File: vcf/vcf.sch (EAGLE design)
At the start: 94 parts, among them IC1 OPA4130U, IC2 OPA4130U, IC3 OPA4130U, IC4 OPA4130U, IC5 OPA4130U, Q1 BC847ASMD, Q2 BC847ASMD, Q3 BC847ASMD, Q4 BC847ASMD, Q5 BC847ASMD, Q6 BC847ASMD

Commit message: added some critical stuff.  sent the board to pcbway for checking.
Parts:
- added R47, R48: 1k, dan:R-US_R0603
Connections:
- new net N$65: FREQ.A, R48.2
- new net N$66: FREQ.E, R47.1
- net +12V: now also R47.2; no longer FREQ.E
- net -12V: now also R48.1; no longer FREQ.A
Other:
- moved on the sheet: FREQ, R25, R44
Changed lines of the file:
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@@
 <part name="R45" library="dan" deviceset="R-US_" device="R0603" value="1k"/>
 <part name="R46" library="dan" deviceset="R-US_" device="R0603" value="1k"/>
+<part name="R47" library="dan" deviceset="R-US_" device="R0603" value="1k"/>
+<part name="R48" library="dan" deviceset="R-US_" device="R0603" value="1k"/>
 </parts>
 <sheets>
@@
 <instance part="R23" gate="G$1" x="-20.32" y="-33.02"/>
 <instance part="R24" gate="G$1" x="-48.26" y="-53.34"/>
-<instance part="R25" gate="G$1" x="-68.58" y="-35.56"/>
+<instance part="R25" gate="G$1" x="-68.58" y="-43.18"/>
 <instance part="R26" gate="G$1" x="-68.58" y="-53.34"/>
 <instance part="MODAMT" gate="G$1" x="-99.06" y="-25.4"/>
@@
 <instance part="GND20" gate="1" x="208.28" y="73.66"/>
 <instance part="GND21" gate="1" x="149.86" y="200.66"/>
-<instance part="FREQ" gate="G$1" x="-78.74" y="-12.7"/>
-<instance part="P-7" gate="1" x="-78.74" y="-25.4"/>
-<instance part="P+9" gate="1" x="-78.74" y="0"/>
-<instance part="R44" gate="G$1" x="-66.04" y="-12.7"/>
+<instance part="FREQ" gate="G$1" x="-78.74" y="-15.24"/>
+<instance part="P-7" gate="1" x="-78.74" y="-40.64"/>
+<instance part="P+9" gate="1" x="-78.74" y="10.16"/>
+<instance part="R44" gate="G$1" x="-66.04" y="-15.24"/>
 <instance part="GAIN1" gate="G$1" x="-99.06" y="5.08"/>
 <instance part="C5" gate="G$1" x="-2.54" y="38.1" rot="R270"/>
@@
 <instance part="R45" gate="G$1" x="205.74" y="66.04" rot="R180"/>
 <instance part="R46" gate="G$1" x="147.32" y="193.04" rot="R180"/>
+<instance part="R47" gate="G$1" x="-78.74" y="0" rot="R90"/>
+<instance part="R48" gate="G$1" x="-78.74" y="-30.48" rot="R90"/>
 </instances>
 <busses>
@@
 </segment>
 <segment>
-<pinref part="FREQ" gate="G$1" pin="E"/>
-<pinref part="P+9" gate="1" pin="+12V"/>
-<wire x1="-78.74" y1="-5.08" x2="-78.74" y2="-2.54" width="0.1524" layer="91"/>
-</segment>
-<segment>
 <pinref part="P+10" gate="1" pin="+12V"/>
 <wire x1="-12.7" y1="154.94" x2="-12.7" y2="152.4" width="0.1524" layer="91"/>
@@
 <pinref part="P+7" gate="1" pin="+12V"/>
 </segment>
+<segment>
+<pinref part="R47" gate="G$1" pin="2"/>
+<pinref part="P+9" gate="1" pin="+12V"/>
+<wire x1="-78.74" y1="7.62" x2="-78.74" y2="5.08" width="0.1524" layer="91"/>
+</segment>
 </net>
 <net name="-12V" class="0">
@@
 <wire x1="-50.8" y1="177.8" x2="-40.64" y2="177.8" width="0.1524" layer="91"/>
 <junction x="-50.8" y="177.8"/>
-</segment>
-<segment>
-<pinref part="P-7" gate="1" pin="-12V"/>
-<pinref part="FREQ" gate="G$1" pin="A"/>
-<wire x1="-78.74" y1="-22.86" x2="-78.74" y2="-20.32" width="0.1524" layer="91"/>
 </segment>
 <segment>
@@
 <pinref part="P-5" gate="1" pin="-12V"/>
 </segment>
+<segment>
+<pinref part="P-7" gate="1" pin="-12V"/>
+<pinref part="R48" gate="G$1" pin="1"/>
+<wire x1="-78.74" y1="-38.1" x2="-78.74" y2="-35.56" width="0.1524" layer="91"/>
+</segment>
 </net>
 <net name="N$17" class="0">
@@
 <wire x1="-63.5" y1="-53.34" x2="-58.42" y2="-53.34" width="0.1524" layer="91"/>
 <junction x="-58.42" y="-53.34"/>
-<wire x1="-58.42" y1="-35.56" x2="-58.42" y2="-53.34" width="0.1524" layer="91"/>
+<wire x1="-58.42" y1="-35.56" x2="-58.42" y2="-43.18" width="0.1524" layer="91"/>
+<wire x1="-58.42" y1="-43.18" x2="-58.42" y2="-53.34" width="0.1524" layer="91"/>
+<wire x1="-53.34" y1="-35.56" x2="-58.42" y2="-35.56" width="0.1524" layer="91"/>
+<pinref part="IC5" gate="B" pin="-IN"/>
 <pinref part="R25" gate="G$1" pin="2"/>
-<wire x1="-63.5" y1="-35.56" x2="-58.42" y2="-35.56" width="0.1524" layer="91"/>
-<wire x1="-53.34" y1="-35.56" x2="-58.42" y2="-35.56" width="0.1524" layer="91"/>
-<junction x="-58.42" y="-35.56"/>
-<pinref part="IC5" gate="B" pin="-IN"/>
+<wire x1="-63.5" y1="-43.18" x2="-58.42" y2="-43.18" width="0.1524" layer="91"/>
+<junction x="-58.42" y="-43.18"/>
 </segment>
 </net>
@@
 <net name="N$40" class="0">
 <segment>
-<pinref part="R25" gate="G$1" pin="1"/>
-<wire x1="-73.66" y1="-35.56" x2="-83.82" y2="-35.56" width="0.1524" layer="91"/>
-<wire x1="-83.82" y1="-35.56" x2="-83.82" y2="-25.4" width="0.1524" layer="91"/>
+<wire x1="-83.82" y1="-43.18" x2="-83.82" y2="-25.4" width="0.1524" layer="91"/>
 <pinref part="MODAMT" gate="G$1" pin="S"/>
 <wire x1="-83.82" y1="-25.4" x2="-93.98" y2="-25.4" width="0.1524" layer="91"/>
+<pinref part="R25" gate="G$1" pin="1"/>
+<wire x1="-73.66" y1="-43.18" x2="-83.82" y2="-43.18" width="0.1524" layer="91"/>
 </segment>
 </net>
@@
 <pinref part="FREQ" gate="G$1" pin="S"/>
 <pinref part="R44" gate="G$1" pin="1"/>
-<wire x1="-73.66" y1="-12.7" x2="-71.12" y2="-12.7" width="0.1524" layer="91"/>
+<wire x1="-73.66" y1="-15.24" x2="-71.12" y2="-15.24" width="0.1524" layer="91"/>
 </segment>
 </net>
 <net name="N$62" class="0">
 <segment>
-<wire x1="-73.66" y1="5.08" x2="-73.66" y2="20.32" width="0.1524" layer="91"/>
+<wire x1="-88.9" y1="5.08" x2="-88.9" y2="20.32" width="0.1524" layer="91"/>
 <pinref part="R20" gate="G$1" pin="1"/>
-<wire x1="-73.66" y1="20.32" x2="-71.12" y2="20.32" width="0.1524" layer="91"/>
+<wire x1="-88.9" y1="20.32" x2="-71.12" y2="20.32" width="0.1524" layer="91"/>
 <pinref part="GAIN1" gate="G$1" pin="S"/>
-<wire x1="-93.98" y1="5.08" x2="-73.66" y2="5.08" width="0.1524" layer="91"/>
+<wire x1="-93.98" y1="5.08" x2="-88.9" y2="5.08" width="0.1524" layer="91"/>
 </segment>
 </net>
@@
 <pinref part="IC5" gate="B" pin="+IN"/>
 <pinref part="R44" gate="G$1" pin="2"/>
-<wire x1="-58.42" y1="-12.7" x2="-60.96" y2="-12.7" width="0.1524" layer="91"/>
-<wire x1="-58.42" y1="-30.48" x2="-58.42" y2="-12.7" width="0.1524" layer="91"/>
+<wire x1="-58.42" y1="-15.24" x2="-60.96" y2="-15.24" width="0.1524" layer="91"/>
+<wire x1="-58.42" y1="-30.48" x2="-58.42" y2="-15.24" width="0.1524" layer="91"/>
 </segment>
 </net>
@@
 </segment>
 </net>
+<net name="N$65" class="0">
+<segment>
+<pinref part="FREQ" gate="G$1" pin="A"/>
+<pinref part="R48" gate="G$1" pin="2"/>
+<wire x1="-78.74" y1="-25.4" x2="-78.74" y2="-22.86" width="0.1524" layer="91"/>
+</segment>
+</net>
+<net name="N$66" class="0">
+<segment>
+<pinref part="FREQ" gate="G$1" pin="E"/>
+<pinref part="R47" gate="G$1" pin="1"/>
+<wire x1="-78.74" y1="-5.08" x2="-78.74" y2="-7.62" width="0.1524" layer="91"/>
+</segment>
+</net>

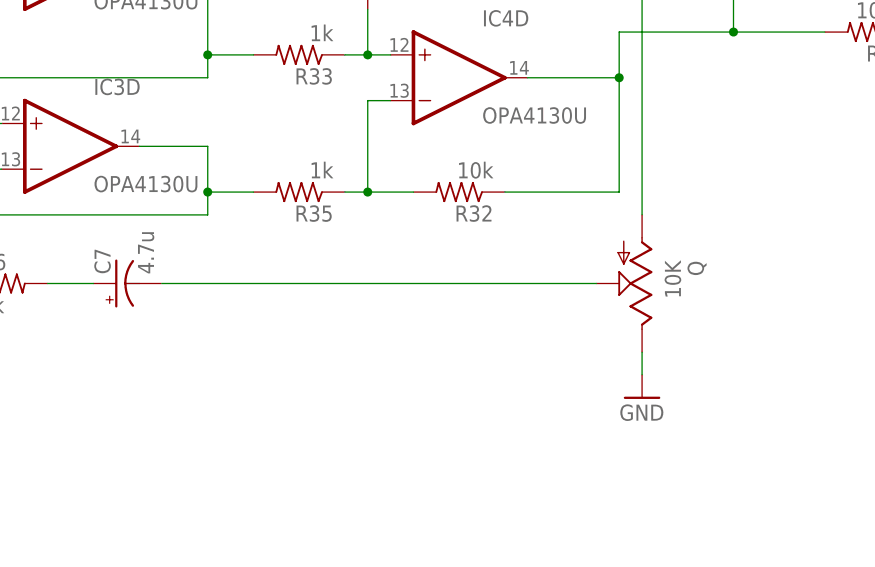
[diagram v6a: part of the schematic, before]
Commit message: fixed polarity on resonance pot.  Sent out to fab.
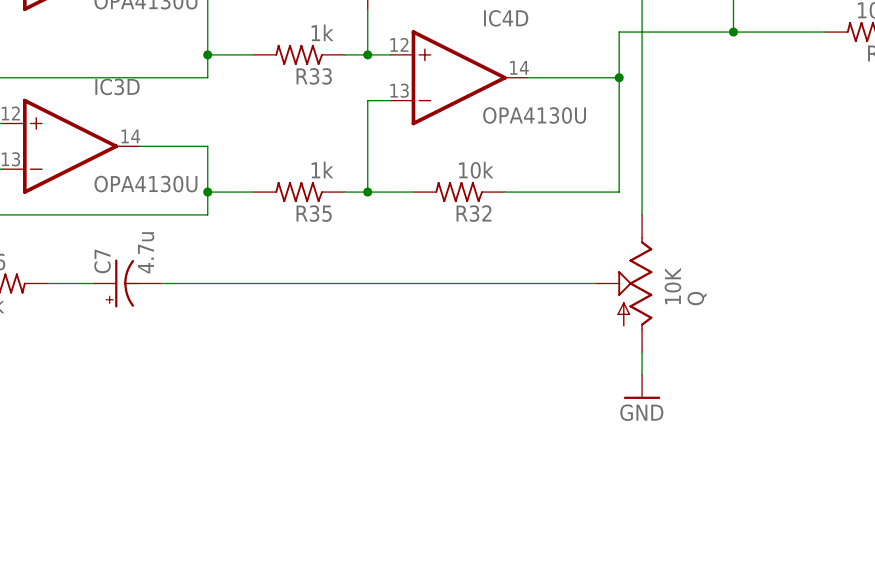
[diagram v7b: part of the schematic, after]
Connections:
- net GND: now also Q.A; no longer Q.E
- net N$27: now also Q.E; no longer Q.A
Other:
- moved on the sheet: Q
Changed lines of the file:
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@@
 <instance part="GND5" gate="1" x="101.6" y="215.9"/>
 <instance part="R16" gate="G$1" x="68.58" y="38.1"/>
-<instance part="Q" gate="G$1" x="139.7" y="38.1" rot="R180"/>
+<instance part="Q" gate="G$1" x="139.7" y="38.1" rot="MR0"/>
 <instance part="R18" gate="G$1" x="-45.72" y="20.32"/>
 <instance part="R19" gate="G$1" x="-66.04" y="35.56"/>
@@
 </segment>
 <segment>
-<pinref part="Q" gate="G$1" pin="E"/>
-<pinref part="GND24" gate="1" pin="GND"/>
-<wire x1="139.7" y1="30.48" x2="139.7" y2="27.94" width="0.1524" layer="91"/>
-</segment>
-<segment>
 <pinref part="GND26" gate="1" pin="GND"/>
 <pinref part="GAIN" gate="G$1" pin="A"/>
@@
 <pinref part="GND10" gate="1" pin="GND"/>
 <wire x1="-142.24" y1="-53.34" x2="-142.24" y2="-55.88" width="0.1524" layer="91"/>
+</segment>
+<segment>
+<pinref part="Q" gate="G$1" pin="A"/>
+<pinref part="GND24" gate="1" pin="GND"/>
+<wire x1="139.7" y1="30.48" x2="139.7" y2="27.94" width="0.1524" layer="91"/>
 </segment>
 </net>
@@
 <pinref part="XPAND" gate="-10" pin="KL"/>
 <wire x1="172.72" y1="160.02" x2="139.7" y2="160.02" width="0.1524" layer="91"/>
-<pinref part="Q" gate="G$1" pin="A"/>
-<wire x1="139.7" y1="45.72" x2="139.7" y2="160.02" width="0.1524" layer="91"/>
-<junction x="139.7" y="160.02"/>
 <wire x1="139.7" y1="190.5" x2="139.7" y2="193.04" width="0.1524" layer="91"/>
 <wire x1="139.7" y1="193.04" x2="139.7" y2="203.2" width="0.1524" layer="91"/>
@@
 <wire x1="142.24" y1="193.04" x2="139.7" y2="193.04" width="0.1524" layer="91"/>
 <junction x="139.7" y="193.04"/>
+<pinref part="Q" gate="G$1" pin="E"/>
+<wire x1="139.7" y1="45.72" x2="139.7" y2="160.02" width="0.1524" layer="91"/>
+<junction x="139.7" y="160.02"/>
 </segment>
 </net>
@@
 </segment>
 </net>
-<net name="N$32" class="0">
-<segment>
-<pinref part="Q" gate="G$1" pin="S"/>
-<wire x1="86.36" y1="38.1" x2="134.62" y2="38.1" width="0.1524" layer="91"/>
-<pinref part="C7" gate="G$1" pin="-"/>
-</segment>
-</net>
 <net name="N$57" class="0">
 <segment>
@@
 </segment>
 </net>
+<net name="N$32" class="0">
+<segment>
+<pinref part="Q" gate="G$1" pin="S"/>
+<pinref part="C7" gate="G$1" pin="-"/>
+<wire x1="134.62" y1="38.1" x2="86.36" y2="38.1" width="0.1524" layer="91"/>
+</segment>
+</net>

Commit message: made some of the post first draft schematic changes
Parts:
- added R49, R50: 1k, dan:R-US_R0603
- R16: value 10k -> 1k
- R23: value 1k -> 100k
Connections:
- removed net N$65 (its old number): FREQ.A, R48.2
- new net N$60: FREQ.A, R47.1
- new net N$68: C6.1, R11.2, R49.1, R5.2, R50.2, R6.2
- net +12V: now also R50.1
- net N$13: now also R49.2; no longer C6.1, R11.2, R5.2, R6.2
- net N$66: now also R48.2; no longer R47.1
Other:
- note added: "Changed this to 50k, but it can be made small by moving them buffers"
- note added: "Freq pot polarity is wrong"
- note added: "Move the buffers after the pots"
- note added: "THis is really far away from the current pair"
- note added: "This was a big screwup"
- moved on the sheet: FREQ, R5
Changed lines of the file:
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@@
 <part name="R15" library="dan" deviceset="R-US_" device="R0603" value="10k"/>
 <part name="GND5" library="dan" deviceset="GND" device=""/>
-<part name="R16" library="dan" deviceset="R-US_" device="R0603" value="10k"/>
+<part name="R16" library="dan" deviceset="R-US_" device="R0603" value="1k"/>
 <part name="Q" library="dan" deviceset="US-EVU" device="F2J" value="10K"/>
 <part name="R18" library="dan" deviceset="R-US_" device="R0603" value="1k"/>
@@
 <part name="R22" library="dan" deviceset="R-US_" device="R0603" value="1k"/>
 <part name="GND9" library="dan" deviceset="GND" device=""/>
-<part name="R23" library="dan" deviceset="R-US_" device="R0603" value="1k"/>
+<part name="R23" library="dan" deviceset="R-US_" device="R0603" value="100k"/>
 <part name="R24" library="dan" deviceset="R-US_" device="R0603" value="1.2k"/>
 <part name="R25" library="dan" deviceset="R-US_" device="R0603" value="10k"/>
@@
 <part name="R47" library="dan" deviceset="R-US_" device="R0603" value="1k"/>
 <part name="R48" library="dan" deviceset="R-US_" device="R0603" value="1k"/>
+<part name="R49" library="dan" deviceset="R-US_" device="R0603" value="1k"/>
+<part name="P+11" library="dan" deviceset="+12V" device=""/>
+<part name="R50" library="dan" deviceset="R-US_" device="R0603" value="1k"/>
 </parts>
 <sheets>
@@
 <text x="2.54" y="208.28" size="3.81" layer="91">Double check this polarity</text>
 <text x="58.42" y="-35.56" size="3.81" layer="91">Double check this polarity</text>
+<text x="-137.16" y="-60.96" size="1.778" layer="91">Move the buffers after the pots</text>
+<text x="-137.16" y="-33.02" size="1.778" layer="91">Move the buffers after the pots</text>
+<text x="-71.12" y="-5.08" size="1.778" layer="91">Freq pot polarity is wrong</text>
+<text x="-68.58" y="-60.96" size="1.778" layer="91">THis is really far away from the current pair</text>
+<text x="-86.36" y="-63.5" size="1.778" layer="91">Changed this to 50k, but it can be made small by moving them buffers</text>
+<text x="-22.86" y="66.04" size="1.778" layer="91">This was a big screwup</text>
 </plain>
 <instances>
@@
 <instance part="R3" gate="G$1" x="20.32" y="142.24" rot="R90"/>
 <instance part="R4" gate="G$1" x="20.32" y="124.46" rot="R90"/>
-<instance part="R5" gate="G$1" x="12.7" y="86.36"/>
+<instance part="R5" gate="G$1" x="12.7" y="55.88"/>
 <instance part="R6" gate="G$1" x="20.32" y="17.78" rot="R90"/>
 <instance part="GND1" gate="1" x="20.32" y="5.08"/>
@@
 <instance part="GND20" gate="1" x="208.28" y="73.66"/>
 <instance part="GND21" gate="1" x="149.86" y="200.66"/>
-<instance part="FREQ" gate="G$1" x="-78.74" y="-15.24"/>
+<instance part="FREQ" gate="G$1" x="-78.74" y="-15.24" rot="MR180"/>
 <instance part="P-7" gate="1" x="-78.74" y="-40.64"/>
 <instance part="P+9" gate="1" x="-78.74" y="10.16"/>
@@
 <instance part="R47" gate="G$1" x="-78.74" y="0" rot="R90"/>
 <instance part="R48" gate="G$1" x="-78.74" y="-30.48" rot="R90"/>
+<instance part="R49" gate="G$1" x="20.32" y="76.2" rot="R90"/>
+<instance part="P+11" gate="1" x="-10.16" y="12.7"/>
+<instance part="R50" gate="G$1" x="-2.54" y="17.78" rot="R90"/>
 </instances>
 <busses>
@@
 <wire x1="55.88" y1="86.36" x2="33.02" y2="86.36" width="0.1524" layer="91"/>
 <junction x="33.02" y="86.36"/>
-<pinref part="R6" gate="G$1" pin="2"/>
-<wire x1="20.32" y1="22.86" x2="20.32" y2="25.4" width="0.1524" layer="91"/>
-<pinref part="R5" gate="G$1" pin="2"/>
-<wire x1="20.32" y1="25.4" x2="20.32" y2="86.36" width="0.1524" layer="91"/>
-<wire x1="20.32" y1="86.36" x2="17.78" y2="86.36" width="0.1524" layer="91"/>
-<pinref part="C6" gate="G$1" pin="1"/>
-<wire x1="7.62" y1="20.32" x2="7.62" y2="25.4" width="0.1524" layer="91"/>
-<wire x1="7.62" y1="25.4" x2="20.32" y2="25.4" width="0.1524" layer="91"/>
-<junction x="20.32" y="25.4"/>
+<pinref part="R49" gate="G$1" pin="2"/>
+<wire x1="20.32" y1="81.28" x2="20.32" y2="86.36" width="0.1524" layer="91"/>
 <junction x="20.32" y="86.36"/>
-<pinref part="R11" gate="G$1" pin="2"/>
-<wire x1="25.4" y1="25.4" x2="20.32" y2="25.4" width="0.1524" layer="91"/>
 </segment>
 </net>
@@
 <pinref part="U$1" gate="G$1" pin="B"/>
 <wire x1="33.02" y1="38.1" x2="5.08" y2="38.1" width="0.1524" layer="91"/>
-<wire x1="5.08" y1="38.1" x2="5.08" y2="86.36" width="0.1524" layer="91"/>
+<pinref part="C5" gate="G$1" pin="+"/>
 <pinref part="R5" gate="G$1" pin="1"/>
-<wire x1="5.08" y1="86.36" x2="7.62" y2="86.36" width="0.1524" layer="91"/>
-<pinref part="C5" gate="G$1" pin="+"/>
-<wire x1="0" y1="38.1" x2="5.08" y2="38.1" width="0.1524" layer="91"/>
+<wire x1="5.08" y1="38.1" x2="0" y2="38.1" width="0.1524" layer="91"/>
+<wire x1="7.62" y1="55.88" x2="5.08" y2="55.88" width="0.1524" layer="91"/>
+<wire x1="5.08" y1="55.88" x2="5.08" y2="38.1" width="0.1524" layer="91"/>
 <junction x="5.08" y="38.1"/>
 </segment>
@@
 <wire x1="-78.74" y1="7.62" x2="-78.74" y2="5.08" width="0.1524" layer="91"/>
 </segment>
+<segment>
+<pinref part="P+11" gate="1" pin="+12V"/>
+<wire x1="-10.16" y1="10.16" x2="-2.54" y2="10.16" width="0.1524" layer="91"/>
+<pinref part="R50" gate="G$1" pin="1"/>
+<wire x1="-2.54" y1="10.16" x2="-2.54" y2="12.7" width="0.1524" layer="91"/>
+</segment>
 </net>
 <net name="-12V" class="0">
@@
 </segment>
 </net>
-<net name="N$60" class="0">
-<segment>
-<pinref part="FREQ" gate="G$1" pin="S"/>
-<pinref part="R44" gate="G$1" pin="1"/>
-<wire x1="-73.66" y1="-15.24" x2="-71.12" y2="-15.24" width="0.1524" layer="91"/>
-</segment>
-</net>
 <net name="N$62" class="0">
 <segment>
@@
 </segment>
 </net>
-<net name="N$65" class="0">
-<segment>
-<pinref part="FREQ" gate="G$1" pin="A"/>
-<pinref part="R48" gate="G$1" pin="2"/>
-<wire x1="-78.74" y1="-25.4" x2="-78.74" y2="-22.86" width="0.1524" layer="91"/>
-</segment>
-</net>
-<net name="N$66" class="0">
-<segment>
-<pinref part="FREQ" gate="G$1" pin="E"/>
-<pinref part="R47" gate="G$1" pin="1"/>
-<wire x1="-78.74" y1="-5.08" x2="-78.74" y2="-7.62" width="0.1524" layer="91"/>
-</segment>
-</net>
 <net name="N$32" class="0">
 <segment>
@@
 </segment>
 </net>
+<net name="N$68" class="0">
+<segment>
+<pinref part="R49" gate="G$1" pin="1"/>
+<wire x1="20.32" y1="71.12" x2="20.32" y2="55.88" width="0.1524" layer="91"/>
+<pinref part="R5" gate="G$1" pin="2"/>
+<wire x1="20.32" y1="55.88" x2="17.78" y2="55.88" width="0.1524" layer="91"/>
+<pinref part="R6" gate="G$1" pin="2"/>
+<wire x1="20.32" y1="22.86" x2="20.32" y2="25.4" width="0.1524" layer="91"/>
+<junction x="20.32" y="25.4"/>
+<pinref part="R11" gate="G$1" pin="2"/>
+<wire x1="25.4" y1="25.4" x2="20.32" y2="25.4" width="0.1524" layer="91"/>
+<wire x1="7.62" y1="25.4" x2="20.32" y2="25.4" width="0.1524" layer="91"/>
+<pinref part="C6" gate="G$1" pin="1"/>
+<wire x1="7.62" y1="20.32" x2="7.62" y2="25.4" width="0.1524" layer="91"/>
+<wire x1="20.32" y1="55.88" x2="20.32" y2="25.4" width="0.1524" layer="91"/>
+<junction x="20.32" y="55.88"/>
+<pinref part="R50" gate="G$1" pin="2"/>
+<wire x1="-2.54" y1="22.86" x2="-2.54" y2="25.4" width="0.1524" layer="91"/>
+<wire x1="-2.54" y1="25.4" x2="7.62" y2="25.4" width="0.1524" layer="91"/>
+<junction x="7.62" y="25.4"/>
+</segment>
+</net>
+<net name="N$60" class="0">
+<segment>
+<pinref part="FREQ" gate="G$1" pin="A"/>
+<pinref part="R47" gate="G$1" pin="1"/>
+<wire x1="-78.74" y1="-7.62" x2="-78.74" y2="-5.08" width="0.1524" layer="91"/>
+</segment>
+</net>
+<net name="N$65" class="0">
+<segment>
+<pinref part="FREQ" gate="G$1" pin="S"/>
+<pinref part="R44" gate="G$1" pin="1"/>
+<wire x1="-73.66" y1="-15.24" x2="-71.12" y2="-15.24" width="0.1524" layer="91"/>
+</segment>
+</net>
+<net name="N$66" class="0">
+<segment>
+<pinref part="FREQ" gate="G$1" pin="E"/>
+<pinref part="R48" gate="G$1" pin="2"/>
+<wire x1="-78.74" y1="-22.86" x2="-78.74" y2="-25.4" width="0.1524" layer="91"/>
+</segment>
+</net>
